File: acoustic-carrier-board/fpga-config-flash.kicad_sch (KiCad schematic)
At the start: 24 parts, among them IC1 ECP5-BGA256, J701 Conn_02x03_Odd_Even, J702 PMOD_JTAG, J703 PMOD_SPI, SW701 SW_Push, U701 W25Q128JVS, U702 W25Q128JVS

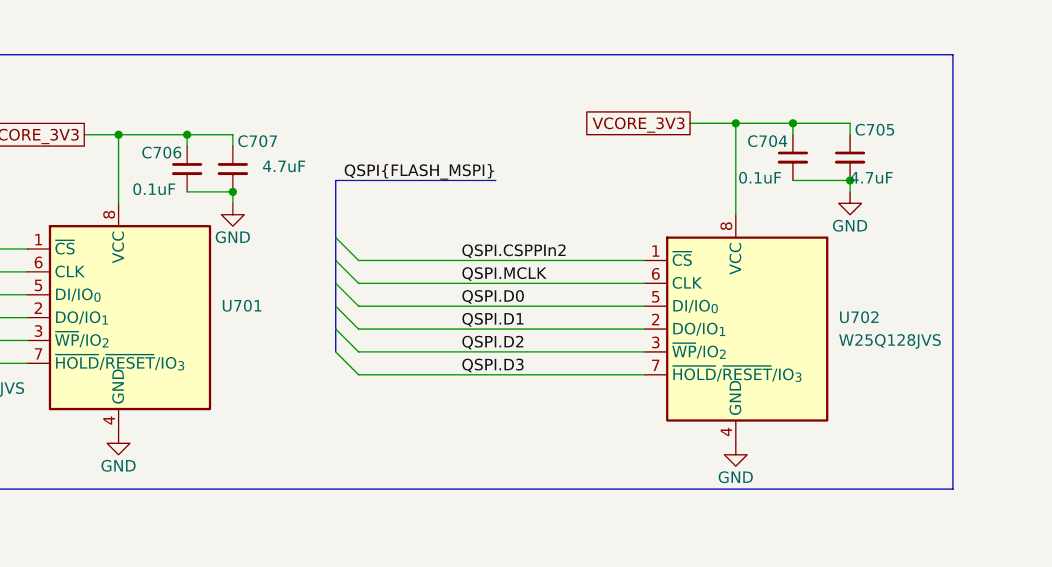
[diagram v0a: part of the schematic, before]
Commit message: Modified readme, removed testpoints and stubs, changed simulation folder structure, removed excess length matching
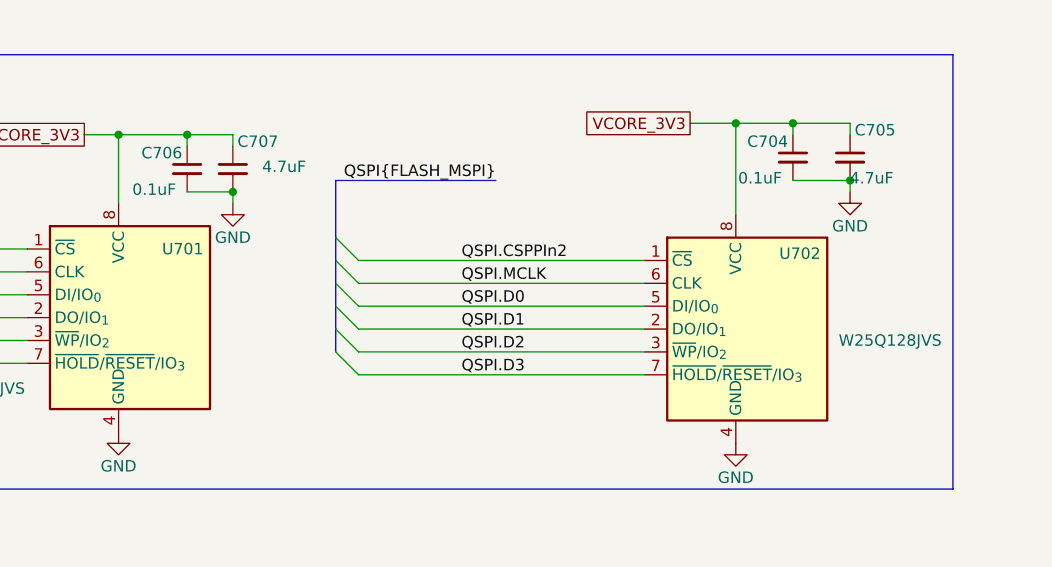
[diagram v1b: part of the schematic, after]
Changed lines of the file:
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@@
 		(on_board yes)
 		(dnp no)
-		(fields_autoplaced yes)
 		(property "Reference" "U702"
-			(at 266.7 153.6699 0)
+			(at 260.096 146.558 0)
 			(effects
 				(font
@@
 		(dnp no)
 		(property "Reference" "U701"
-			(at 198.12 152.3999 0)
-			(effects
-				(font
+			(at 191.516 146.05 0)
+			(effects
+				(font

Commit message: added step-files
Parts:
- C701, C705, C707: LCSC Part Number (none) -> C23733; LPN C23733 -> (none); MPN CL05A475MP5NRNC -> (none); Manufacturing Part Number (none) -> CL05A475MP5NRNC
- C702, C704, C706, C708: LCSC Part Number (none) -> C22435929; LPN C22435929 -> (none); MPN CGA0201X7R104K160ET -> (none); Manufacturing Part Number (none) -> CGA0201X7R104K160ET
- C703: LCSC Part Number (none) -> C285010; LPN C285010 -> (none); MPN 0201B103K250NT -> (none); Manufacturing Part Number (none) -> 0201B103K250NT
- IC1: LCSC Part Number (none) -> C1521614; LPN C1521614 -> (none); MPN LFE5U-25F-6BG256C -> (none); Manufacturing Part Number (none) -> LFE5U-25F-6BG256C
- J701: now left out of the parts list
- J702, J703: LCSC Part Number (none) -> C2897426; LPN C2897426 -> (none); MPN PM254-2-06-W-8.5 -> (none); Manufacturing Part Number (none) -> PM254-2-06-W-8.5
- R701: LCSC Part Number (none) -> C25117; LPN C25117 -> (none); MPN 0402WGF4700TCE -> (none); Manufacturing Part Number (none) -> 0402WGF4700TCE
- R704, R705, R707: LCSC Part Number (none) -> C25900; LPN C25900 -> (none); MPN 0402WGF4701TCE -> (none); Manufacturing Part Number (none) -> 0402WGF4701TCE
- R706: LCSC Part Number (none) -> C11702; LPN C11702 -> (none); MPN 0402WGF1001TCE -> (none); Manufacturing Part Number (none) -> 0402WGF1001TCE
- RN703, RN704, RN708: LCSC Part Number (none) -> C1980; LPN C1980 -> (none); MPN 4D03WGJ0472T5E -> (none); Manufacturing Part Number (none) -> 4D03WGJ0472T5E
- RN707: LCSC Part Number (none) -> C29718; LPN C29718 -> (none); MPN 4D03WGJ0103T5E -> (none); Manufacturing Part Number (none) -> 4D03WGJ0103T5E
- SW701: LCSC Part Number (none) -> C720477; LPN C720477 -> (none); MPN TS-1088-AR02016 -> (none); Manufacturing Part Number (none) -> TS-1088-AR02016
- U701, U702: LCSC Part Number (none) -> C113767; LPN C113767 -> (none); MPN W25Q128JVSIQ -> (none); Manufacturing Part Number (none) -> W25Q128JVSIQ
